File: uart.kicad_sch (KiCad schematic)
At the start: 65 parts, among them J2 GPIO, J3 UART0, J4 UART1, J5 UART2, J6 UART3_HV, U10 TVS4201MR6, U11 TVS4201MR6, U12 TVS4201MR6, U13 TVS4201MR6, U14 TVS4201MR6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

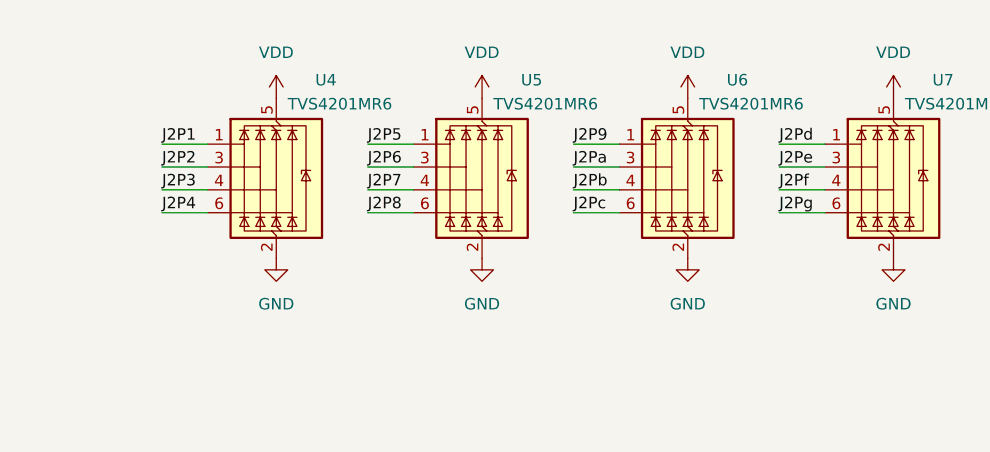
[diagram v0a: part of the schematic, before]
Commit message: Renumber TVS diodes' legs to ease PCB routing
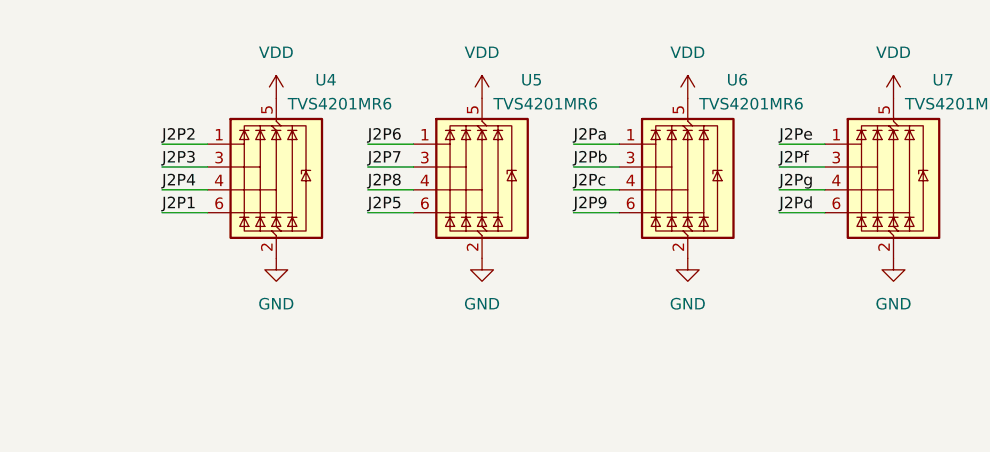
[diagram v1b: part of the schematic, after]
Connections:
- net J2P1: now also U4.6 (I/O4); no longer U4.1 (I/O1)
- net J2P2: now also U4.1 (I/O1); no longer U4.3 (I/O2)
- net J2P3: now also U4.3 (I/O2); no longer U4.4 (I/O3)
- net J2P4: now also U4.4 (I/O3); no longer U4.6 (I/O4)
- net J2P5: now also U5.6 (I/O4); no longer U5.1 (I/O1)
- net J2P6: now also U5.1 (I/O1); no longer U5.3 (I/O2)
- net J2P7: now also U5.3 (I/O2); no longer U5.4 (I/O3)
- net J2P8: now also U5.4 (I/O3); no longer U5.6 (I/O4)
- net J2P9: now also U6.6 (I/O4); no longer U6.1 (I/O1)
- net J2Pa: now also U6.1 (I/O1); no longer U6.3 (I/O2)
- net J2Pb: now also U6.3 (I/O2); no longer U6.4 (I/O3)
- net J2Pc: now also U6.4 (I/O3); no longer U6.6 (I/O4)
- net J2Pd: now also U7.6 (I/O4); no longer U7.1 (I/O1)
- net J2Pe: now also U7.1 (I/O1); no longer U7.3 (I/O2)
- net J2Pf: now also U7.3 (I/O2); no longer U7.4 (I/O3)
- net J2Pg: now also U7.4 (I/O3); no longer U7.6 (I/O4)
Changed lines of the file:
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@@
 		)
 	)
-	(label "J2Pf"
+	(label "J2Pg"
 		(at 148.59 40.64 0)
 		(fields_autoplaced yes)
@@
 		)
 	)
-	(label "J2Pb"
+	(label "J2Pc"
 		(at 125.73 40.64 0)
 		(fields_autoplaced yes)
@@
 		)
 	)
-	(label "J2Pa"
+	(label "J2Pb"
 		(at 125.73 38.1 0)
 		(fields_autoplaced yes)
@@
 		)
 	)
-	(label "J2P8"
+	(label "J2P5"
 		(at 102.87 43.18 0)
 		(fields_autoplaced yes)
@@
 		)
 	)
-	(label "J2Pc"
+	(label "J2P9"
 		(at 125.73 43.18 0)
 		(fields_autoplaced yes)
@@
 		)
 	)
-	(label "J2Pg"
+	(label "J2Pd"
 		(at 148.59 43.18 0)
 		(fields_autoplaced yes)
@@
 		)
 	)
-	(label "J2P3"
+	(label "J2P4"
 		(at 80.01 40.64 0)
 		(fields_autoplaced yes)
@@
 		)
 	)
-	(label "J2Pe"
+	(label "J2Pf"
 		(at 148.59 38.1 0)
 		(fields_autoplaced yes)
@@
 		)
 	)
-	(label "J2P6"
+	(label "J2P7"
 		(at 102.87 38.1 0)
 		(fields_autoplaced yes)
@@
 		)
 	)
-	(label "J2P7"
+	(label "J2P8"
 		(at 102.87 40.64 0)
 		(fields_autoplaced yes)
@@
 		)
 	)
-	(label "J2Pd"
+	(label "J2Pe"
 		(at 148.59 35.56 0)
 		(fields_autoplaced yes)
@@
 		)
 	)
-	(label "J2P9"
+	(label "J2Pa"
 		(at 125.73 35.56 0)
 		(fields_autoplaced yes)
@@
 		)
 	)
-	(label "J2P1"
+	(label "J2P2"
 		(at 80.01 35.56 0)
 		(fields_autoplaced yes)
@@
 		)
 	)
-	(label "J2P2"
+	(label "J2P3"
 		(at 80.01 38.1 0)
 		(fields_autoplaced yes)
@@
 		)
 	)
-	(label "J2P5"
+	(label "J2P6"
 		(at 102.87 35.56 0)
 		(fields_autoplaced yes)
@@
 		)
 	)
-	(label "J2P4"
+	(label "J2P1"
 		(at 80.01 43.18 0)
 		(fields_autoplaced yes)
